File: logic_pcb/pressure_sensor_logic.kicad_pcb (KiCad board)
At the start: 2 copper layers, 34 x 34 mm, 24 parts, among them J11 TYPE-C-31-M-12, J2 Conn_01x02_Pin, J3 Conn_01x04_Pin, J4 Conn_01x02_Pin, J5 Conn_01x02_Pin, J6 Conn_01x02_Pin, SW2 SW_Push, U3 AP2112K-3.3, U4 STM32G030F6Px, U5 CH340E

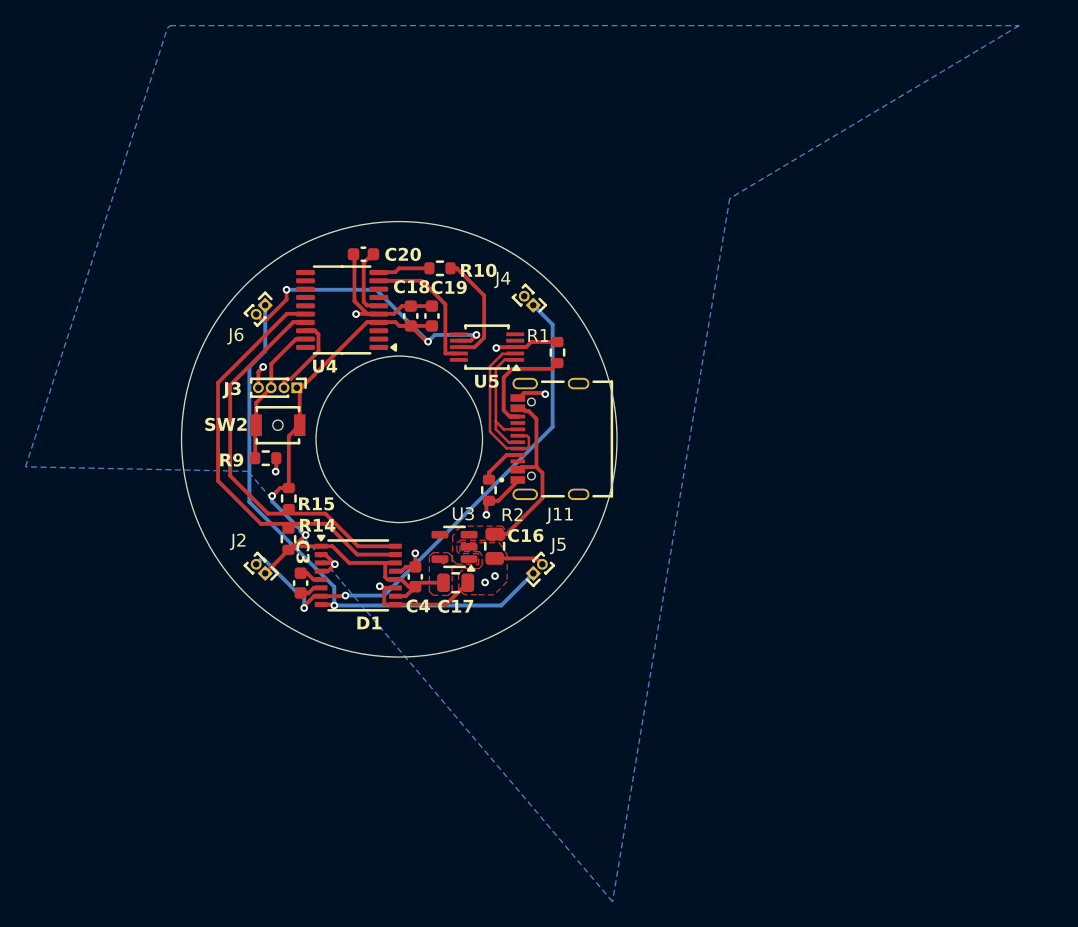
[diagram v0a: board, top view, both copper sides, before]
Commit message: mounting_holes_added
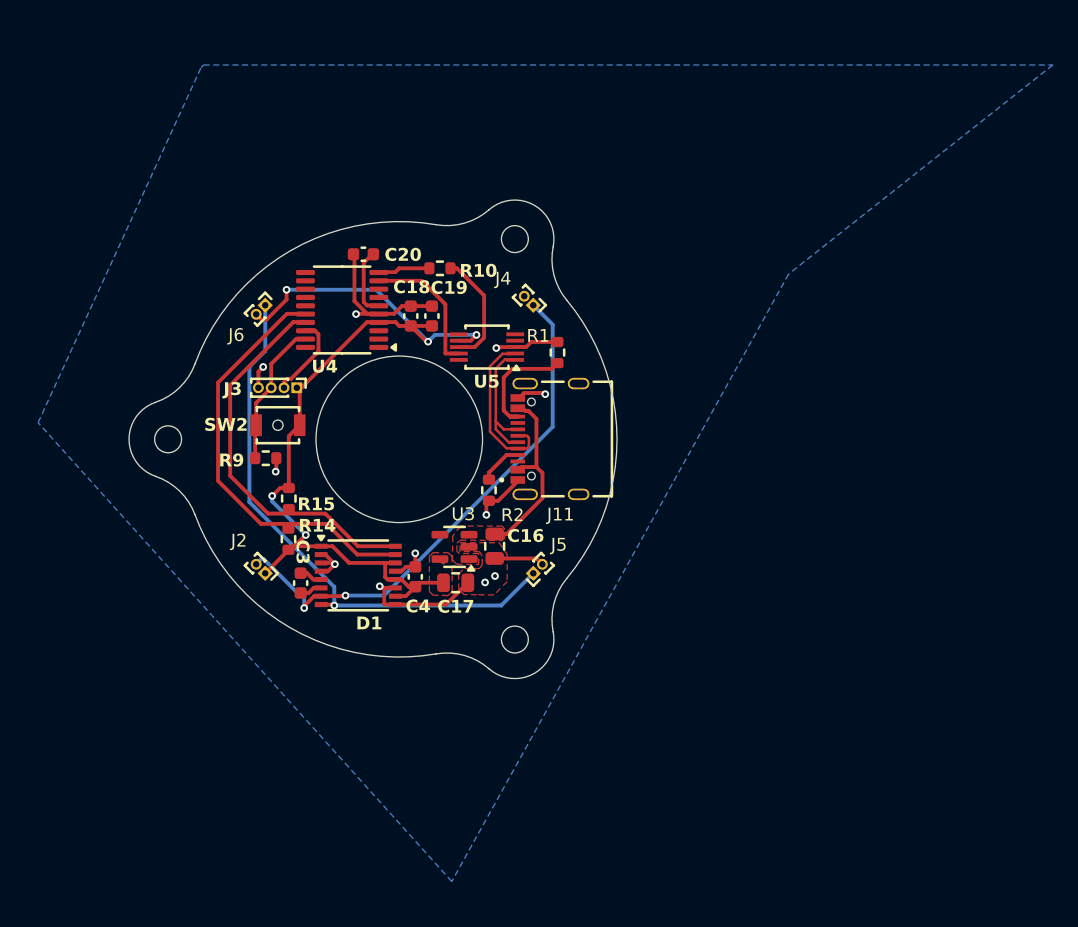
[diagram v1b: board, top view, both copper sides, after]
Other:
- board size 34 x 34 mm -> 38.1 x 37.4 mm
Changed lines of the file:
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@@
 		)
+	)
+	(gr_arc
+		(start 52.872134 66.705623)
+		(mid 55.075204 66.821805)
+		(end 57.013843 67.87475)
+		(stroke
+			(width 0.1)
+			(type default)
+		)
+		(layer "Edge.Cuts")
+	)
+	(gr_arc
+		(start 34.053124 44.059544)
+		(mid 32.850993 45.909389)
+		(end 30.969776 47.061806)
+		(stroke
+			(width 0.1)
+			(type default)
+		)
+		(layer "Edge.Cuts")
+	)
+	(gr_arc
+		(start 57.013843 32.025257)
+		(mid 55.075214 33.078238)
+		(end 52.872134 33.194384)
+		(stroke
+			(width 0.1)
+			(type default)
+		)
+		(layer "Edge.Cuts")
+	)
+	(gr_arc
+		(start 63.074708 39.084843)
+		(mid 62.073761 37.118845)
+		(end 62.016347 34.913454)
+		(stroke
+			(width 0.1)
+			(type default)
+		)
+		(layer "Edge.Cuts")
 	)
 	(gr_circle
-		(center 50.000002 49.950003)
-		(end 67.000002 49.950003)
+		(center 59.024989 65.581762)
+		(end 60.074989 65.581762)
 		(stroke
 			(width 0.1)
@@
 	)
 	(gr_circle
-		(center 50.000002 49.950003)
-		(end 56.500002 49.950003)
+		(center 49.999989 49.950003)
+		(end 56.499989 49.950003)
+		(stroke
+			(width 0.1)
+			(type default)
+		)
+		(fill none)
+		(layer "Edge.Cuts")
+	)
+	(gr_arc
+		(start 30.969776 52.8382)
+		(mid 32.85098 53.99063)
+		(end 34.053124 55.840462)
+		(stroke
+			(width 0.1)
+			(type default)
+		)
+		(layer "Edge.Cuts")
+	)
+	(gr_arc
+		(start 34.053124 44.059544)
+		(mid 41.499987 35.227568)
+		(end 52.872134 33.194384)
+		(stroke
+			(width 0.1)
+			(type default)
+		)
+		(layer "Edge.Cuts")
+	)
+	(gr_arc
+		(start 62.016347 64.986552)
+		(mid 60.550004 68.223165)
+		(end 57.013843 67.87475)
+		(stroke
+			(width 0.1)
+			(type default)
+		)
+		(layer "Edge.Cuts")
+	)
+	(gr_arc
+		(start 52.872134 66.705623)
+		(mid 41.499988 64.672436)
+		(end 34.053124 55.840462)
+		(stroke
+			(width 0.1)
+			(type default)
+		)
+		(layer "Edge.Cuts")
+	)
+	(gr_arc
+		(start 63.074708 39.084843)
+		(mid 66.999991 49.950003)
+		(end 63.074708 60.815164)
+		(stroke
+			(width 0.1)
+			(type default)
+		)
+		(layer "Edge.Cuts")
+	)
+	(gr_arc
+		(start 62.016347 64.986552)
+		(mid 62.073761 62.781162)
+		(end 63.074708 60.815164)
+		(stroke
+			(width 0.1)
+			(type default)
+		)
+		(layer "Edge.Cuts")
+	)
+	(gr_arc
+		(start 30.969776 52.8382)
+		(mid 28.899994 49.950003)
+		(end 30.969776 47.061806)
+		(stroke
+			(width 0.1)
+			(type default)
+		)
+		(layer "Edge.Cuts")
+	)
+	(gr_circle
+		(center 31.949989 49.950003)
+		(end 32.999989 49.950003)
+		(stroke
+			(width 0.1)
+			(type default)
+		)
+		(fill none)
+		(layer "Edge.Cuts")
+	)
+	(gr_arc
+		(start 57.013843 32.025257)
+		(mid 60.549957 31.67692)
+		(end 62.016347 34.913454)
+		(stroke
+			(width 0.1)
+			(type default)
+		)
+		(layer "Edge.Cuts")
+	)
+	(gr_circle
+		(center 59.024989 34.318245)
+		(end 60.074989 34.318245)
 		(stroke
 			(width 0.1)
@@
 		(polygon
 			(pts
-				(xy 32.100002 17.650003) (xy 98.400002 17.650003) (xy 75.800002 31.150003) (xy 66.650002 86.050003)
-				(xy 38.200002 52.450003) (xy 20.825002 52.100003) (xy 31.900002 17.850003)
+				(xy 34.725002 20.725003) (xy 101.025002 20.725003) (xy 80.400002 37.050003) (xy 54.100002 84.475003)
+				(xy 21.800002 48.650003) (xy 34.525002 20.925003)
 			)
 		)
 	)
+	(group ""
+		(members "29e8d2bb-6849-4540-a55f-1de5bd489f15" "4835bfaa-e548-4d86-be31-7f9163df4251"
+			"54bbfd39-deb8-4521-961e-f27826872150" "55770a7b-752a-4367-9a78-8c8b789b85c6"
+			"5c40e9d8-f8c5-4824-93d5-f6dc4accf154" "641b232f-8666-487a-8ffe-daffa39d248d"
+			"719b6a0c-7bec-4c09-80fd-615f219c6812" "92be1d32-5286-4db1-9d95-4b2df327fa6b"
+			"93c9ea90-bcf2-45bd-9a5e-aa4c4bf7b168" "97ade62b-e95b-48a9-a91e-94dc2332e528"
+			"a350c17f-fad1-4678-8e3e-b09a22198878" "ca0cf9ec-5e32-456a-9e14-226602f04a6b"
+			"d1a8ebf9-109b-40ba-805b-37c2fcb0dd25" "d39f5ed8-f321-4e73-a130-04178187bb83"
+			"e7c664d0-057a-4212-9dd1-90587beb871d" "ec959206-30cb-4c10-8b73-1c3f57dfaf2e"
+		)
+	)

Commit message: alignement_corrected
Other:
- board text added: "+3.3V"
- board text added: "A+"
- board text added: "A-"
- board text added: "GND"
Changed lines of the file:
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@@
 		(layer "B.Fab")
+	)
+	(gr_text "+3.3V"
+		(at 44.375002 63.025003 0)
+		(layer "B.SilkS")
+		(effects
+			(font
+				(size 1 1)
+				(thickness 0.2)
+				(bold yes)
+			)
+			(justify left bottom mirror)
+		)
+	)
+	(gr_text "A-"
+		(at 41.750002 37.700003 0)
+		(layer "B.SilkS")
+		(effects
+			(font
+				(size 1 1)
+				(thickness 0.2)
+				(bold yes)
+			)
+			(justify left bottom mirror)
+		)
+	)
+	(gr_text "A-"
+		(at 60.025002 62.625003 0)
+		(layer "B.SilkS")
+		(effects
+			(font
+				(size 1 1)
+				(thickness 0.2)
+				(bold yes)
+			)
+			(justify left bottom mirror)
+		)
+	)
+	(gr_text "A+"
+		(at 38.150002 58.400003 0)
+		(layer "B.SilkS")
+		(effects
+			(font
+				(size 1 1)
+				(thickness 0.2)
+				(bold yes)
+			)
+			(justify left bottom mirror)
+		)
+	)
+	(gr_text "GND"
+		(at 59.300002 37.900003 0)
+		(layer "B.SilkS")
+		(effects
+			(font
+				(size 1 1)
+				(thickness 0.2)
+				(bold yes)
+			)
+			(justify left bottom mirror)
+		)
+	)
+	(gr_text "+3.3V"
+		(at 40.175002 42.925003 0)
+		(layer "B.SilkS")
+		(effects
+			(font
+				(size 1 1)
+				(thickness 0.2)
+				(bold yes)
+			)
+			(justify left bottom mirror)
+		)
+	)
+	(gr_text "GND"
+		(at 64.350002 58.550003 0)
+		(layer "B.SilkS")
+		(effects
+			(font
+				(size 1 1)
+				(thickness 0.2)
+				(bold yes)
+			)
+			(justify left bottom mirror)
+		)
+	)
+	(gr_text "A+"
+		(at 63.175002 41.350003 0)
+		(layer "B.SilkS")
+		(effects
+			(font
+				(size 1 1)
+				(thickness 0.2)
+				(bold yes)
+			)
+			(justify left bottom mirror)
+		)
 	)
 	(segment

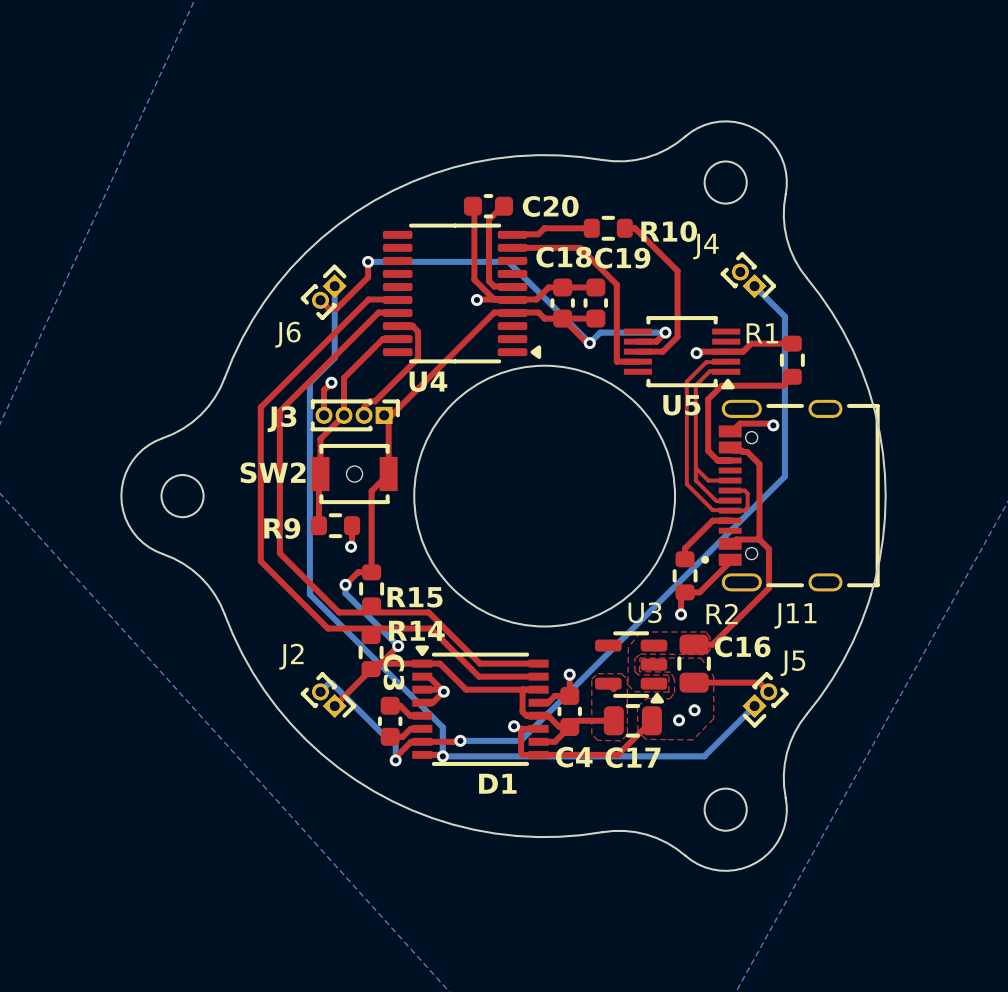
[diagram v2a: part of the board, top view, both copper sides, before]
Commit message: 3d_start_point_added
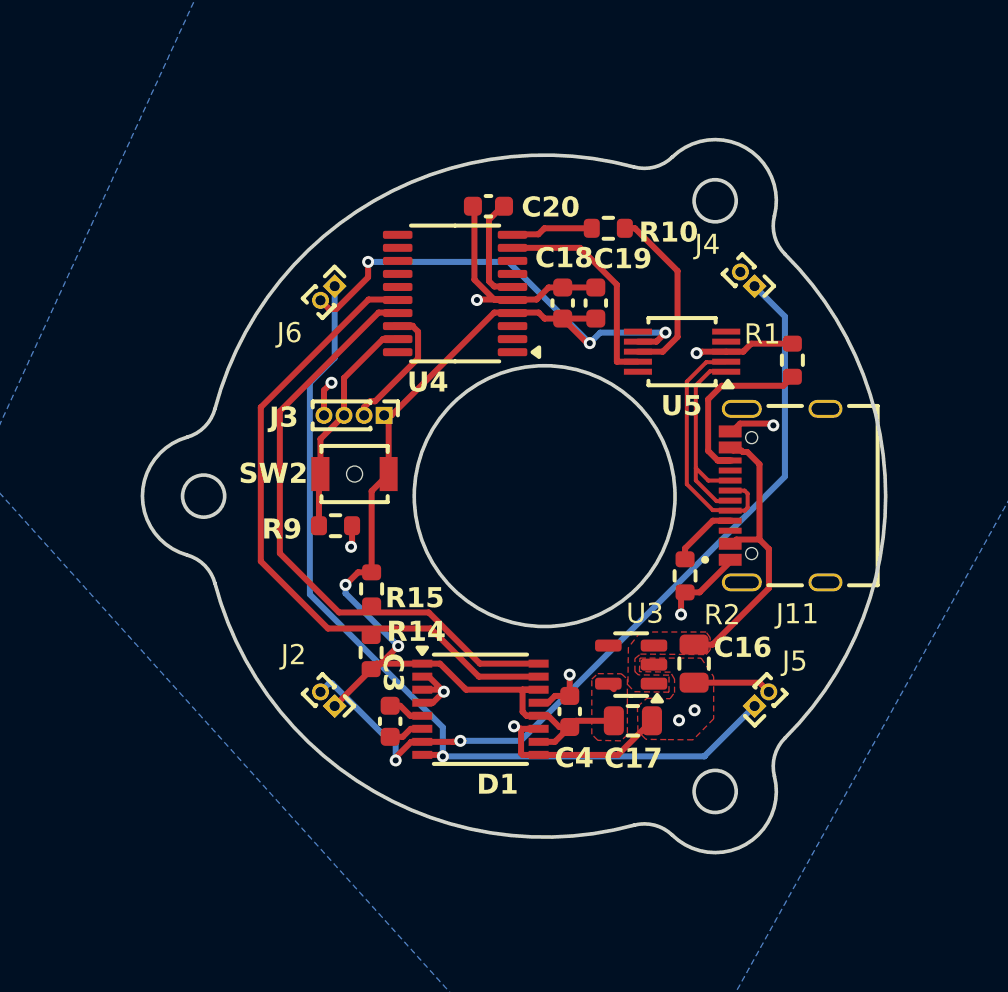
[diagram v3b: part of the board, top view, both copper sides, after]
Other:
- board size 38.1 x 37.4 mm -> 37.1 x 35.5 mm
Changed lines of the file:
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@@
 	)
 	(gr_arc
-		(start 52.872134 66.705623)
-		(mid 55.075204 66.821805)
-		(end 57.013843 67.87475)
-		(stroke
-			(width 0.1)
+		(start 54.450223 66.357182)
+		(mid 41.5 64.672437)
+		(end 33.565857 54.299588)
+		(stroke
+			(width 0.18)
 			(type default)
 		)
@@
 	)
 	(gr_arc
-		(start 34.053124 44.059544)
-		(mid 32.850993 45.909389)
-		(end 30.969776 47.061806)
-		(stroke
-			(width 0.1)
+		(start 54.450223 66.357182)
+		(mid 55.476432 66.351639)
+		(end 56.370303 66.855754)
+		(stroke
+			(width 0.18)
 			(type default)
 		)
 		(layer "Edge.Cuts")
 	)
-	(gr_arc
-		(start 57.013843 32.025257)
-		(mid 55.075214 33.078238)
-		(end 52.872134 33.194384)
-		(stroke
-			(width 0.1)
-			(type default)
-		)
-		(layer "Edge.Cuts")
-	)
-	(gr_arc
-		(start 63.074708 39.084843)
-		(mid 62.073761 37.118845)
-		(end 62.016347 34.913454)
-		(stroke
-			(width 0.1)
-			(type default)
-		)
-		(layer "Edge.Cuts")
-	)
 	(gr_circle
-		(center 59.024989 65.581762)
-		(end 60.074989 65.581762)
-		(stroke
-			(width 0.1)
+		(center 58.500002 64.672435)
+		(end 59.550002 64.672435)
+		(stroke
+			(width 0.18)
 			(type default)
 		)
@@
 		(layer "Edge.Cuts")
 	)
+	(gr_arc
+		(start 56.370303 33.044252)
+		(mid 55.476434 33.548379)
+		(end 54.450223 33.542824)
+		(stroke
+			(width 0.18)
+			(type default)
+		)
+		(layer "Edge.Cuts")
+	)
 	(gr_circle
-		(center 49.999989 49.950003)
-		(end 56.499989 49.950003)
-		(stroke
-			(width 0.1)
+		(center 33.000002 49.950003)
+		(end 34.050002 49.950003)
+		(stroke
+			(width 0.18)
 			(type default)
 		)
@@
 	)
 	(gr_arc
-		(start 30.969776 52.8382)
-		(mid 32.85098 53.99063)
-		(end 34.053124 55.840462)
-		(stroke
-			(width 0.1)
+		(start 33.565857 45.600419)
+		(mid 41.500002 35.227575)
+		(end 54.450223 33.542824)
+		(stroke
+			(width 0.18)
 			(type default)
 		)
@@
 	)
 	(gr_arc
-		(start 34.053124 44.059544)
-		(mid 41.499987 35.227568)
-		(end 52.872134 33.194384)
-		(stroke
-			(width 0.1)
+		(start 56.370303 33.044252)
+		(mid 60.024964 32.586219)
+		(end 61.455661 35.980285)
+		(stroke
+			(width 0.18)
 			(type default)
 		)
 		(layer "Edge.Cuts")
 	)
-	(gr_arc
-		(start 62.016347 64.986552)
-		(mid 60.550004 68.223165)
-		(end 57.013843 67.87475)
-		(stroke
-			(width 0.1)
-			(type default)
-		)
-		(layer "Edge.Cuts")
-	)
-	(gr_arc
-		(start 52.872134 66.705623)
-		(mid 41.499988 64.672436)
-		(end 34.053124 55.840462)
-		(stroke
-			(width 0.1)
-			(type default)
-		)
-		(layer "Edge.Cuts")
-	)
-	(gr_arc
-		(start 63.074708 39.084843)
-		(mid 66.999991 49.950003)
-		(end 63.074708 60.815164)
-		(stroke
-			(width 0.1)
-			(type default)
-		)
-		(layer "Edge.Cuts")
-	)
-	(gr_arc
-		(start 62.016347 64.986552)
-		(mid 62.073761 62.781162)
-		(end 63.074708 60.815164)
-		(stroke
-			(width 0.1)
-			(type default)
-		)
-		(layer "Edge.Cuts")
-	)
-	(gr_arc
-		(start 30.969776 52.8382)
-		(mid 28.899994 49.950003)
-		(end 30.969776 47.061806)
-		(stroke
-			(width 0.1)
-			(type default)
-		)
-		(layer "Edge.Cuts")
-	)
 	(gr_circle
-		(center 31.949989 49.950003)
-		(end 32.999989 49.950003)
-		(stroke
-			(width 0.1)
+		(center 50.000002 49.950003)
+		(end 56.500002 49.950003)
+		(stroke
+			(width 0.18)
 			(type default)
 		)
@@
 	)
 	(gr_arc
-		(start 57.013843 32.025257)
-		(mid 60.549957 31.67692)
-		(end 62.016347 34.913454)
-		(stroke
-			(width 0.1)
+		(start 32.174042 52.886036)
+		(mid 29.94995 49.949983)
+		(end 32.174042 47.01397)
+		(stroke
+			(width 0.18)
 			(type default)
 		)
 		(layer "Edge.Cuts")
 	)
+	(gr_arc
+		(start 61.455661 63.919721)
+		(mid 61.466032 62.893559)
+		(end 61.983925 62.007598)
+		(stroke
+			(width 0.18)
+			(type default)
+		)
+		(layer "Edge.Cuts")
+	)
+	(gr_arc
+		(start 33.565857 45.600419)
+		(mid 33.057545 46.491897)
+		(end 32.174042 47.01397)
+		(stroke
+			(width 0.18)
+			(type default)
+		)
+		(layer "Edge.Cuts")
+	)
+	(gr_arc
+		(start 61.983925 37.892409)
+		(mid 67.000002 49.950004)
+		(end 61.983925 62.007598)
+		(stroke
+			(width 0.18)
+			(type default)
+		)
+		(layer "Edge.Cuts")
+	)
+	(gr_arc
+		(start 61.455661 63.919721)
+		(mid 60.025001 67.313883)
+		(end 56.370303 66.855754)
+		(stroke
+			(width 0.18)
+			(type default)
+		)
+		(layer "Edge.Cuts")
+	)
 	(gr_circle
-		(center 59.024989 34.318245)
-		(end 60.074989 34.318245)
-		(stroke
-			(width 0.1)
+		(center 58.500002 35.227571)
+		(end 59.550002 35.227571)
+		(stroke
+			(width 0.18)
 			(type default)
 		)
 		(fill none)
+		(layer "Edge.Cuts")
+	)
+	(gr_arc
+		(start 61.983925 37.892409)
+		(mid 61.46601 37.00646)
+		(end 61.455661 35.980285)
+		(stroke
+			(width 0.18)
+			(type default)
+		)
+		(layer "Edge.Cuts")
+	)
+	(gr_arc
+		(start 32.174042 52.886036)
+		(mid 33.057565 53.408083)
+		(end 33.565857 54.299588)
+		(stroke
+			(width 0.18)
+			(type default)
+		)
 		(layer "Edge.Cuts")
 	)
@@
 	)
 	(group ""
-		(members "29e8d2bb-6849-4540-a55f-1de5bd489f15" "4835bfaa-e548-4d86-be31-7f9163df4251"
-			"54bbfd39-deb8-4521-961e-f27826872150" "55770a7b-752a-4367-9a78-8c8b789b85c6"
-			"5c40e9d8-f8c5-4824-93d5-f6dc4accf154" "641b232f-8666-487a-8ffe-daffa39d248d"
-			"719b6a0c-7bec-4c09-80fd-615f219c6812" "92be1d32-5286-4db1-9d95-4b2df327fa6b"
-			"93c9ea90-bcf2-45bd-9a5e-aa4c4bf7b168" "97ade62b-e95b-48a9-a91e-94dc2332e528"
-			"a350c17f-fad1-4678-8e3e-b09a22198878" "ca0cf9ec-5e32-456a-9e14-226602f04a6b"
-			"d1a8ebf9-109b-40ba-805b-37c2fcb0dd25" "d39f5ed8-f321-4e73-a130-04178187bb83"
-			"e7c664d0-057a-4212-9dd1-90587beb871d" "ec959206-30cb-4c10-8b73-1c3f57dfaf2e"
-		)
-	)
+		(members "02658e6c-a4da-474c-ba46-641dbe7d89de" "02b23530-128e-4d92-8852-42ef44e3a59d"
+			"0f55499e-c410-456f-bc4a-8ee33d8318ce" "259d9ad5-40c0-4960-b6aa-e437ed5c4fc0"
+			"328412f4-c572-4f45-980f-5a3510f6a6aa" "340ecf9e-7ef3-41b6-a324-08b151df6976"
+			"4446380d-38f5-43a3-986d-5273f22dcae2" "564251aa-52ce-4e4d-8b86-e4554e3c114c"
+			"6c39b75f-f61b-4721-a81a-14baedd94830" "815dd8f9-bfe1-4fea-a333-9d1da5ca1914"
+			"8a6eb41c-6442-4a1f-8e4b-5bc20f795a4e" "d1fae160-8734-461d-a0e5-2e945316784e"
+			"e29616a8-1a09-4032-b28c-3155a41a14c2" "e7f1b13f-f3a3-4ebe-89d8-c9ed46941e5c"
+			"e8d1cb56-40f1-4ca7-8861-d4f3a4ae98d9" "ee665297-2dd3-4f81-9a3d-80cf16b30cbf"
+		)
+	)
